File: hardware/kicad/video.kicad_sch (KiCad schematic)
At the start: 27 parts, among them J1 Conn_Coaxial, Q1 BC327, Q2 BC337, U12 74HC245, U13 74HC165, U2 74HC4040, U5 ATF22LV10CQZ, U6 ATF22LV10CQZ, U7 74HC163, U8 74HC163, U9 AS6C6264-55PIN

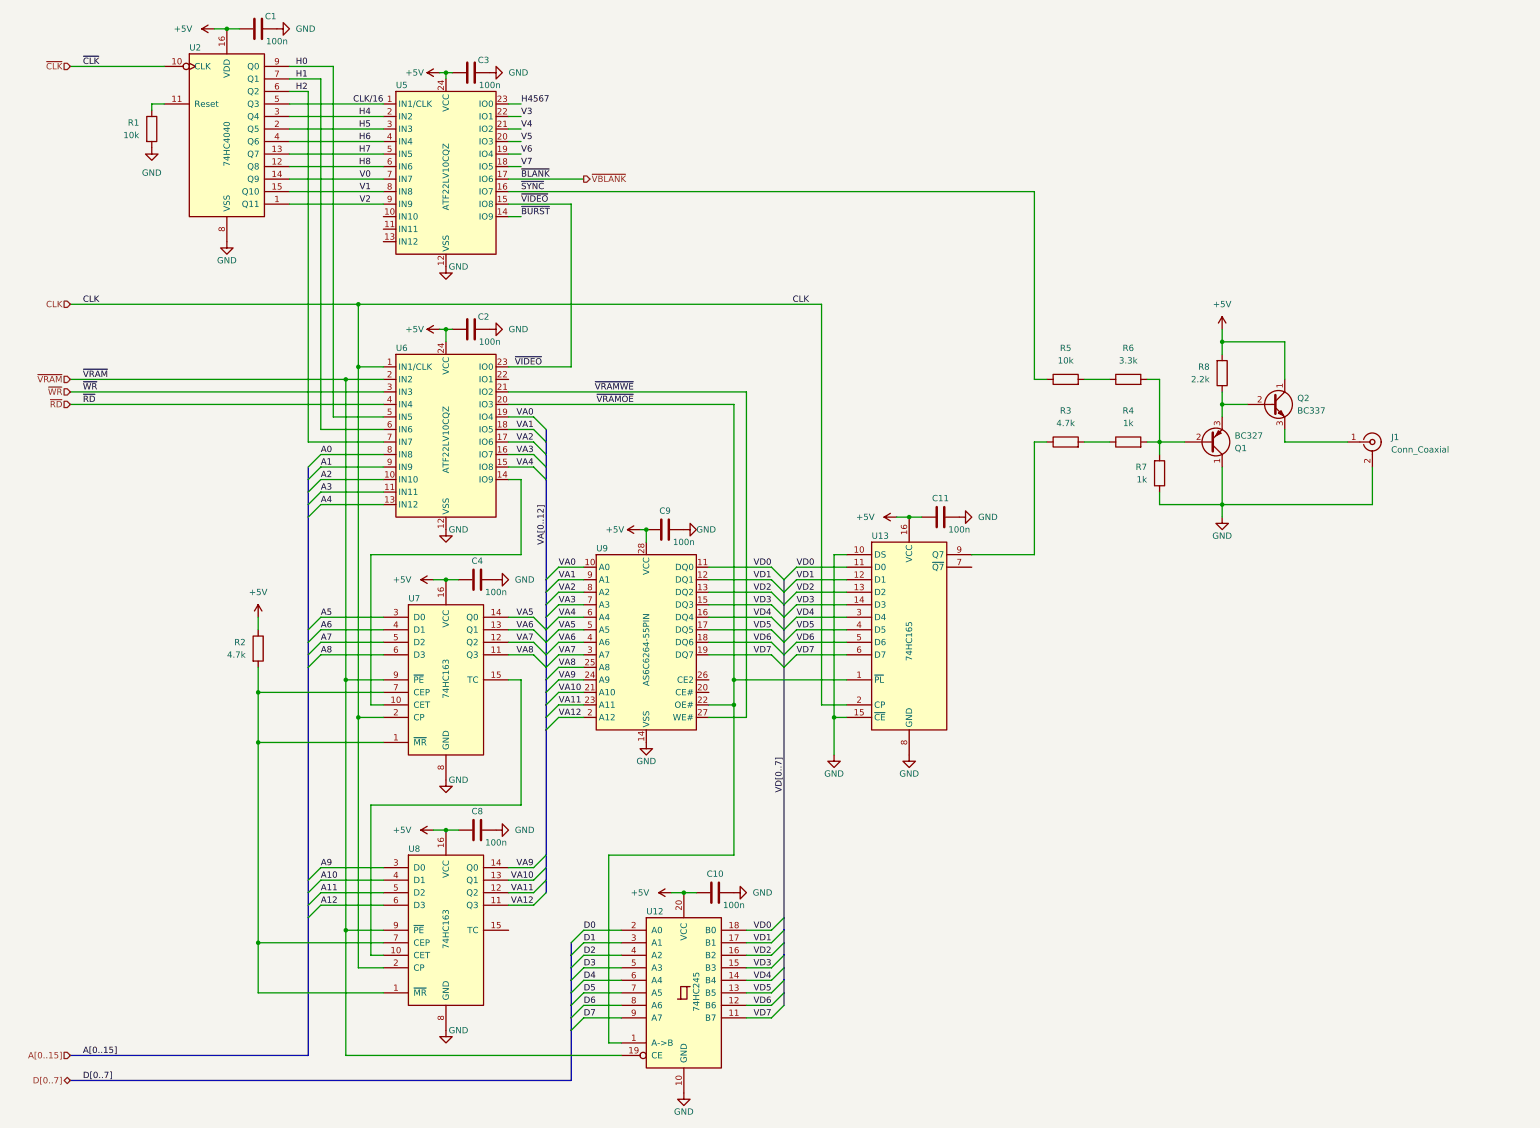
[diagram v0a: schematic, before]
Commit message: Update schematic to reflect current state
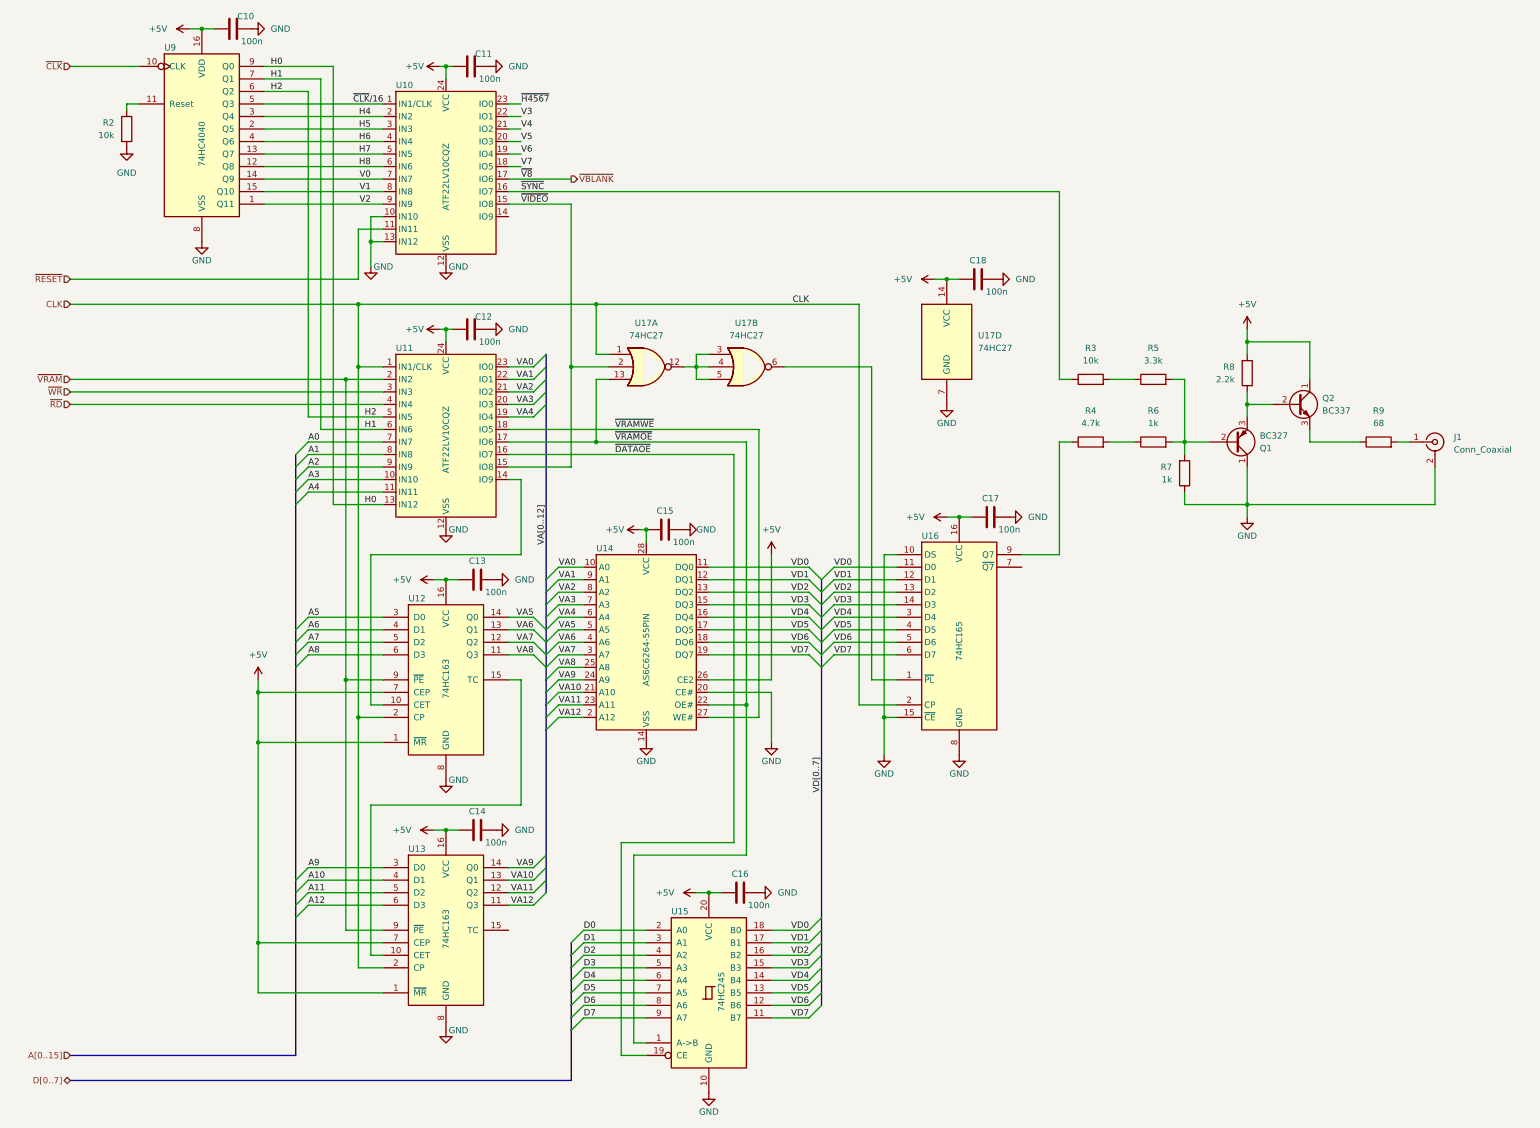
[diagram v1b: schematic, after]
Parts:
- removed R2: 4.7k, symbol Device:R
- added C18: 100n, symbol Device:C
- added R9: 68, symbol Device:R
- added U17: 74HC27, symbol 74xx_SK:74HC27
- renumbered C1 to C10, C3 to C11, C2 to C12, C4 to C13, C8 to C14, C9 to C15, C10 to C16, C11 to C17, R1 to R2, R5 to R3, R3 to R4, R6 to R5, R4 to R6, U5 to U10, U6 to U11, U7 to U12, U8 to U13, U9 to U14, U12 to U15, U13 to U16, U2 to U9
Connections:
- net +5V: now also U12.1 (~{MR}), U12.7 (CEP), U13.1 (~{MR}), U13.7 (CEP), U14.26 (CE2), C18.1, U17.14 (VCC)
- net A0: now also U11.7 (IN7); no longer U11.8 (IN8)
- net A1: now also U11.8 (IN8); no longer U11.9 (IN9)
- net A2: now also U11.9 (IN9); no longer U11.10 (IN10)
- net A3: now also U11.10 (IN10); no longer U11.11 (IN11)
- net A4: now also U11.11 (IN11); no longer U11.13 (IN12)
- net CLK: now also U17.1
- net GND: now also U10.10 (IN10), U10.13 (IN12), U14.20 (CE#), C18.2, U17.7 (GND)
- net H0: now also U11.13 (IN12); no longer U11.5 (IN5)
- net H2: now also U11.5 (IN5); no longer U11.7 (IN7)
- net VA0: now also U11.23 (IO0); no longer U11.19 (IO4)
- net VA1: now also U11.22 (IO1); no longer U11.18 (IO5)
- net VA2: now also U11.21 (IO2); no longer U11.17 (IO6)
- net VA3: now also U11.20 (IO3); no longer U11.16 (IO7)
- net VA4: now also U11.19 (IO4); no longer U11.15 (IO8)
- net ~{VIDEO}: now also U11.15 (IO8), U17.2; no longer U11.23 (IO0)
- net ~{VRAMOE}: now also U11.17 (IO6), U17.13; no longer U11.20 (IO3), U16.1 (~{PL})
- net ~{VRAMWE}: now also U11.18 (IO5); no longer U11.21 (IO2)
- net ~{VRAM}: no longer U15.19 (CE)
- net ~{RESET}: now reaches U10.11 (IN11)
- net at J1.1 (In): now also R9.2; no longer Q2.3 (E)
- net CLK/16 renamed ~{CLK}/16
- net H4567 renamed ~{H4567}
- net ~{BURST}: no longer names the net of U10.14 (IO9)
- new net: U16.1 (~{PL}), U17.6
- new net: Q2.3 (E), R9.1
- new net: U17.12, U17.3, U17.4, U17.5
- new net ~{DATAOE}: U11.16 (IO7), U15.19 (CE)
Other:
- moved on the sheet: C10, C11, C16, C17, J1, Q1, Q2, R2, R3, R4, R5, R6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

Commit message: Add titles to schematic sheets
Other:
- title: (none) -> Z80 SBC Video
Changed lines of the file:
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@@
 (kicad_sch (version 20230121) (generator eeschema)
   (paper "A3")
+  (title_block
+    (title "Z80 SBC Video")
+  )
   (junction (at 152.4 144.78) (diameter 0) (color 0 0 0 0)
   )
